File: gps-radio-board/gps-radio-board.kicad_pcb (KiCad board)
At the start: 2 copper layers, 32 x 48 mm, 10 parts, among them J1 Conn_Coaxial_Small, J2 Conn_01x02, J3 USB_C_Receptacle_USB2.0_16P, J4 Conn_Coaxial_Small, U1 ESP32-C6-MINI-1U-H4, U3 AP2112K-3.3, U4 AP2112K-3.3

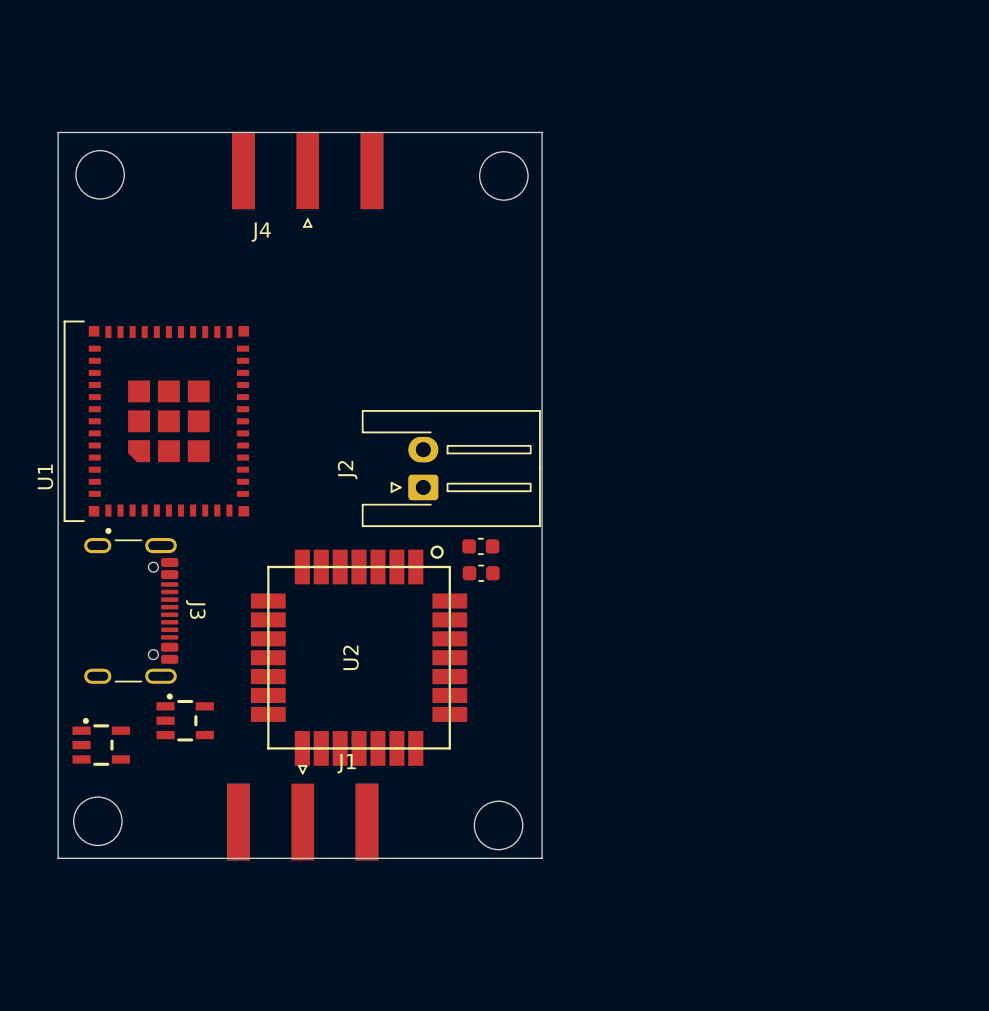
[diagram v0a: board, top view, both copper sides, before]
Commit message: Add components to schematic
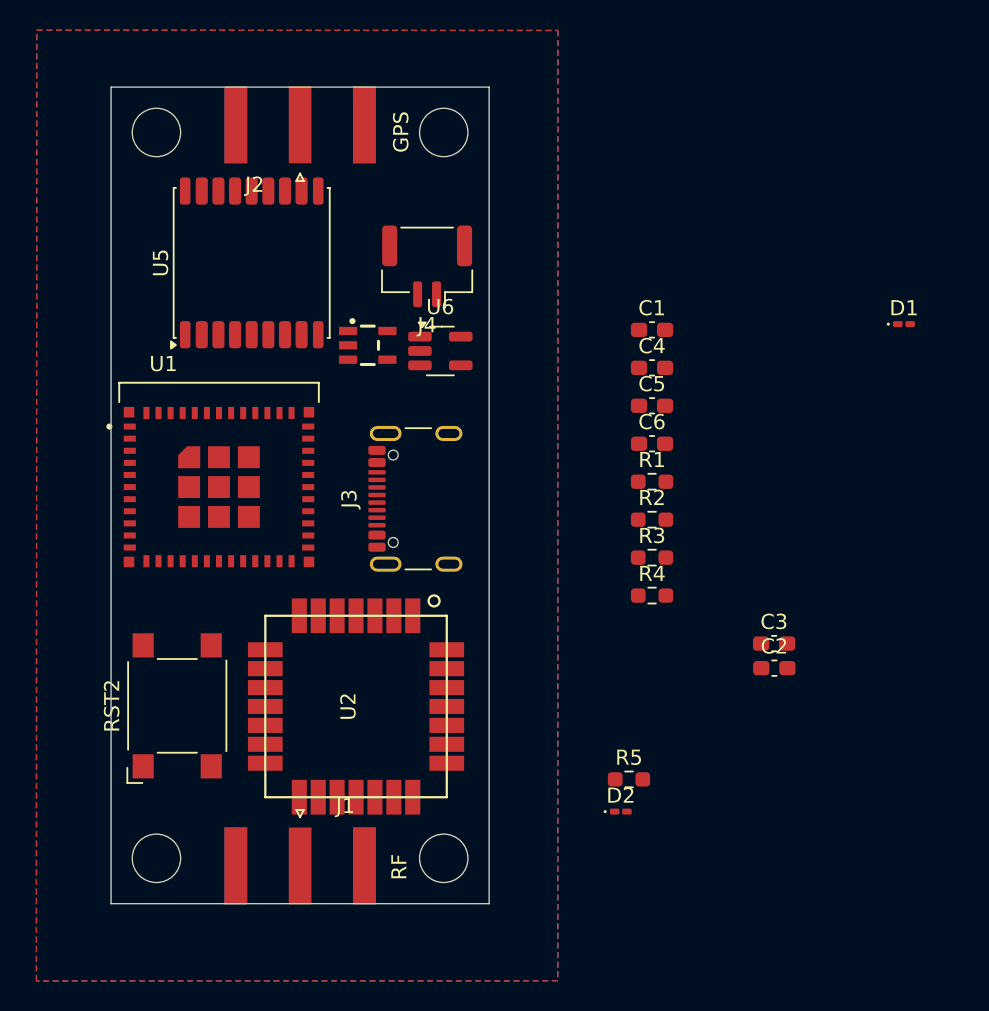
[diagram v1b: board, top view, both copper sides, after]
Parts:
- removed U3: AP2112K-3.3, PCM_SparkFun-Semiconductor-Standard:SOT23-5
- added C1: 4.7u, Capacitor_SMD:C_0603_1608Metric_Pad1.08x0.95mm_HandSolder, F.Cu at (123.3, 89.1)
- added C4: 4.7u, Capacitor_SMD:C_0603_1608Metric_Pad1.08x0.95mm_HandSolder, F.Cu at (123.3, 91.6)
- added C5: 4.7u, Capacitor_SMD:C_0603_1608Metric_Pad1.08x0.95mm_HandSolder, F.Cu at (123.3, 94.1)
- added C6: 4.7u, Capacitor_SMD:C_0603_1608Metric_Pad1.08x0.95mm_HandSolder, F.Cu at (123.3, 96.6)
- added D1: LED, LED_SMD:LED_0201_0603Metric_Pad0.64x0.40mm_HandSolder, F.Cu at (139.9, 88.7)
- added D2: LED, LED_SMD:LED_0201_0603Metric_Pad0.64x0.40mm_HandSolder, F.Cu at (121.2, 120.9)
- added R1: 2k, Resistor_SMD:R_0603_1608Metric_Pad0.98x0.95mm_HandSolder, F.Cu at (123.3, 99.1)
- added R2: 470, Resistor_SMD:R_0603_1608Metric_Pad0.98x0.95mm_HandSolder, F.Cu at (123.3, 101.6)
- added R3: 5.1k, Resistor_SMD:R_0603_1608Metric_Pad0.98x0.95mm_HandSolder, F.Cu at (123.3, 104.1)
- added R4: 5.1k, Resistor_SMD:R_0603_1608Metric_Pad0.98x0.95mm_HandSolder, F.Cu at (123.3, 106.6)
- added R5: 470, Resistor_SMD:R_0603_1608Metric_Pad0.98x0.95mm_HandSolder, F.Cu at (121.8, 118.8)
- added RST2: SW_Omron_B3FS, Button_Switch_SMD:SW_SPST_Omron_B3FS-100xP, F.Cu at (91.9, 113.9)
- added U5: MAX-M10N, gps-radio-board:ublox_MAX, F.Cu at (96.8, 84.6)
- added U6: MCP73831, Package_TO_SOT_SMD:SOT-23-5_HandSoldering, F.Cu at (109.3, 90.5)
- C2: value 10u -> 100n; footprint PCM_SparkFun-Capacitor:C_0603_1608Metric -> Capacitor_SMD:C_0603_1608Metric_Pad1.08x0.95mm_HandSolder
- C3: value 100n -> 10u; footprint PCM_SparkFun-Capacitor:C_0603_1608Metric -> Capacitor_SMD:C_0603_1608Metric_Pad1.08x0.95mm_HandSolder
- J1: value Conn_Coaxial_Small -> SMA
- J2: value Conn_01x02 -> SMA; footprint Connector_JST:JST_XH_S2B-XH-A-1_1x02_P2.50mm_Horizontal -> Connector_Coaxial:SMA_Amphenol_132289_EdgeMount
- J4: value Conn_Coaxial_Small -> JST_BATT; footprint Connector_Coaxial:SMA_Amphenol_132289_EdgeMount -> Connector_JST:JST_GH_SM02B-GHS-TB_1x02-1MP_P1.25mm_Horizontal
- moved U4 27.6 mm to (104.5, 90.1)
- moved J2 25.3 mm to (100.0, 75.5)
- moved J3 22.3 mm to (108.8, 100.2), turned to 90 degrees
- moved C3 20.4 mm to (131.3, 109.8)
- moved C2 20.4 mm to (131.4, 111.4)
- moved J4 10.1 mm to (108.4, 84.8), turned to 180 degrees
- moved U1 5.47 mm to (94.6, 99.5), turned to 0 degrees
- moved U2 3.23 mm to (103.7, 114.0)
- moved J1 2.91 mm to (100.0, 124.5)
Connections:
- net Net-(J3-VBUS-PadA4) renamed /USB_IN
- C2 pad 1: unconnected-(C2-Pad1) -> +3V3
- C2 pad 2: unconnected-(C2-Pad2) -> GND
- C3 pad 1: unconnected-(C3-Pad1) -> +3V3
- C3 pad 2: unconnected-(C3-Pad2) -> GND
- J2 pad 1: GND -> Net-(J2-In)
- J2 pad 2: Net-(J2-Pin_2) -> GND
- J3 pad A1: Net-(J3-GND-PadA1) -> GND
- J3 pad A12: Net-(J3-GND-PadA1) -> GND
- J3 pad A5: unconnected-(J3-CC1-PadA5) -> Net-(J3-CC1)
- J3 pad A6: unconnected-(J3-D+-PadA6) -> /USB_D+
- J3 pad A7: unconnected-(J3-D--PadA7) -> /USB_D-
- J3 pad B1: Net-(J3-GND-PadA1) -> GND
- J3 pad B12: Net-(J3-GND-PadA1) -> GND
- J3 pad B5: unconnected-(J3-CC2-PadB5) -> Net-(J3-CC2)
- J3 pad B6: unconnected-(J3-D+-PadB6) -> /USB_D+
- J3 pad B7: unconnected-(J3-D--PadB7) -> /USB_D-
- J3 pad SH: unconnected-(J3-SHIELD-PadSH) -> GND
- J4 pad 1: unconnected-(J4-In-Pad1) -> GND
- J4 pad 2: unconnected-(J4-Ext-Pad2) -> +BATT
- U1 pad 17: unconnected-(U1-IO12-Pad17) -> /USB_D-
- U1 pad 18: unconnected-(U1-IO13-Pad18) -> /USB_D+
- U1 pad 30: unconnected-(U1-RXD0-Pad30) -> /WIO_UART_2_TX
- U1 pad 31: unconnected-(U1-TXD0-Pad31) -> /WIO_UART_2_RX
- U1 pad 6: unconnected-(U1-IO3-Pad6) -> Net-(D2-A)
- U2 pad 10: unconnected-(U2-PB6-Pad10) -> /WIO_UART_1_TX
- U2 pad 11: unconnected-(U2-PB5-Pad11) -> /SPI-COTI
- U2 pad 12: unconnected-(U2-PC1-Pad12) -> /I2C-2-SCA
- U2 pad 13: unconnected-(U2-PC0-Pad13) -> /I2C-2-SCL
- U2 pad 18: unconnected-(U2-PA3-Pad18) -> /WIO_UART_2_RX
- U2 pad 19: unconnected-(U2-PA2-Pad19) -> /WIO_UART_2_TX
- U2 pad 20: unconnected-(U2-PB10-Pad20) -> /EXT_INT_GPS
- U2 pad 23: unconnected-(U2-PA0-Pad23) -> /SPI-CS
- U2 pad 3: unconnected-(U2-PA13-Pad3) -> /SWD-WIO-IO
- U2 pad 4: unconnected-(U2-PA14-Pad4) -> /SWD-WIO-CLK
- U2 pad 5: unconnected-(U2-PB15-Pad5) -> /I2C-1-SCL
- U2 pad 6: unconnected-(U2-PA15-Pad6) -> /I2C-1-SDA
- U2 pad 7: unconnected-(U2-PB4-Pad7) -> /SPI-CITO
- U2 pad 8: unconnected-(U2-PB3-Pad8) -> /SPI-SCK
- U2 pad 9: unconnected-(U2-PB7-Pad9) -> /WIO_UART_1_RX
- U4 pad 1: unconnected-(U4-VIN-Pad1) -> +BATT
- U4 pad 2: unconnected-(U4-GND-Pad2) -> GND
- U4 pad 3: unconnected-(U4-EN-Pad3) -> +BATT
- U4 pad 5: unconnected-(U4-VOUT-Pad5) -> +3V3
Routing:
- added copper zone on In2.Cu, net +3V3
- added copper zone on B.Cu, net GND
- added copper zone on F.Cu, net GND
- added copper zone on In1.Cu, net GND
- added copper zone on In2.Cu, net GND
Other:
- board size 32 x 48 mm -> 25 x 54 mm
- copper layers 2 -> 4
- board text added: "GPS"
- board text added: "RF"

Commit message: Inital components in schematic
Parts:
- added C10: 22u, Capacitor_SMD:C_0603_1608Metric_Pad1.08x0.95mm_HandSolder, F.Cu at (136.8, 103.8)
- added C7: 1u, Capacitor_SMD:C_0603_1608Metric_Pad1.08x0.95mm_HandSolder, F.Cu at (136.8, 96.3)
- added C8: 100n, Capacitor_SMD:C_0603_1608Metric_Pad1.08x0.95mm_HandSolder, F.Cu at (136.8, 98.8)
- added C9: 100n, Capacitor_SMD:C_0603_1608Metric_Pad1.08x0.95mm_HandSolder, F.Cu at (136.8, 101.3)
- added R6: 10k, Resistor_SMD:R_0603_1608Metric_Pad0.98x0.95mm_HandSolder, F.Cu at (136.8, 106.3)
- added R7: 10k, Resistor_SMD:R_0603_1608Metric_Pad0.98x0.95mm_HandSolder, F.Cu at (136.8, 108.9)
- added U7: AP2112K-3.3, PCM_SparkFun-Semiconductor-Standard:SOT23-5, F.Cu at (141.7, 97.4)
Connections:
- C6 pad 1: +3V3_G -> +3V3_E
- RST2 pad 1: unconnected-(RST2-Pad1) -> GND
- RST2 pad 2: unconnected-(RST2-Pad2) -> Net-(U1-EN)
- U1 pad 22: unconnected-(U1-IO8-Pad22) -> Net-(U1-IO8)
- U1 pad 3: +3V3 -> +3V3_E
- U1 pad 5: unconnected-(U1-IO2-Pad5) -> Net-(U1-IO2)
- U1 pad 8: unconnected-(U1-EN-Pad8) -> Net-(U1-EN)
- U4 pad 3: +BATT -> Net-(U1-IO2)

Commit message: Inital rousting
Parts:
- removed RST2: SW_Omron_B3FS, Button_Switch_SMD:SW_SPST_Omron_B3FS-100xP
- added C11: 15p, Capacitor_SMD:C_0603_1608Metric_Pad1.08x0.95mm_HandSolder, F.Cu at (101.5, 96.3)
- added C12: 15p, Capacitor_SMD:C_0603_1608Metric_Pad1.08x0.95mm_HandSolder, F.Cu at (101.4, 102.7)
- added D3: 40V@1A, Diode_SMD:D_SOD-123, F.Cu at (103.7, 81.4)
- added D4: 40V@1A, Diode_SMD:D_SOD-123, F.Cu at (108.0, 88.2)
- added J5: Conn_01x04, Connector_JST:JST_SH_BM04B-SRSS-TB_1x04-1MP_P1.00mm_Vertical, F.Cu at (91.9, 113.7)
- added J6: Conn_01x04, Connector_JST:JST_SH_BM04B-SRSS-TB_1x04-1MP_P1.00mm_Vertical, F.Cu at (91.8, 119.0)
- added J7: Conn_01x04, Connector_PinHeader_2.54mm:PinHeader_1x04_P2.54mm_Vertical, F.Cu at (89.4, 90.3)
- added R8: 22, Resistor_SMD:R_0603_1608Metric_Pad0.98x0.95mm_HandSolder, F.Cu at (102.3, 98.7)
- added R9: 22, Resistor_SMD:R_0603_1608Metric_Pad0.98x0.95mm_HandSolder, F.Cu at (102.3, 100.2)
- D1, D2: footprint LED_SMD:LED_0201_0603Metric_Pad0.64x0.40mm_HandSolder -> LED_SMD:LED_0603_1608Metric_Pad1.05x0.95mm_HandSolder
- moved C8 49.0 mm to (89.0, 109.3), turned to 90 degrees
- moved C7 48.8 mm to (89.2, 106.8)
- moved C9 45.6 mm to (91.7, 107.8), turned to 90 degrees
- moved R6 45.4 mm to (91.6, 110.3)
- moved C10 43.8 mm to (93.2, 107.8), turned to 90 degrees
- moved R7 38.9 mm to (101.4, 92.8), turned to 90 degrees
- moved U7 38.5 mm to (103.7, 90.9), turned to -90 degrees
- moved C3 29.4 mm to (102.3, 105.7), turned to 180 degrees
- moved D2 29.1 mm to (95.8, 106.9), turned to 180 degrees
- moved D1 28.8 mm to (111.1, 89.5), turned to 90 degrees
- moved R5 28.0 mm to (95.7, 108.5), turned to 180 degrees
- moved C5 24.5 mm to (99.0, 91.4), turned to 180 degrees
- moved R4 22.7 mm to (103.1, 96.3), turned to 90 degrees
- moved C2 20.6 mm to (111.1, 107.5), turned to 90 degrees
- moved R3 20.2 mm to (103.2, 102.8), turned to -90 degrees
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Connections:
- C4 pad 1: +BATT -> Net-(D3-K)
- C5 pad 1: +BATT -> Net-(D3-K)
- J3 pad A6: /USB_D+ -> Net-(J3-D+-PadA6)
- J3 pad A7: /USB_D- -> Net-(J3-D--PadA7)
- J3 pad B6: /USB_D+ -> Net-(J3-D+-PadA6)
- J3 pad B7: /USB_D- -> Net-(J3-D--PadA7)
- U1 pad 10: unconnected-(U1-IO5-Pad10) -> Net-(J7-Pin_3)
- U1 pad 9: unconnected-(U1-IO4-Pad9) -> Net-(J7-Pin_2)
- U4 pad 1: +BATT -> Net-(D3-K)
- U7 pad 1: +BATT -> Net-(D3-K)
- U7 pad 3: +BATT -> Net-(D3-K)
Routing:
- net +3V3_E: track 0.00 -> 43.5 mm
- net Net-(U1-IO2): track 0.00 -> 41.9 mm, vias 0 -> 2
- net /EXT_INT_GPS: track 0.00 -> 37.2 mm, vias 0 -> 2
- net /WIO_UART_2_TX: track 0.00 -> 33.9 mm, vias 0 -> 2
- net /WIO_UART_2_RX: track 0.00 -> 32.8 mm, vias 0 -> 2
- net /WIO_UART_1_TX: track 0.00 -> 30.2 mm, vias 0 -> 2
- net /WIO_UART_1_RX: track 0.00 -> 29.0 mm, vias 0 -> 2
- net /USB_IN: track 0.00 -> 28.7 mm
- net /SWD-WIO-IO: track 0.00 -> 26.0 mm, vias 0 -> 2
- net /SWD-WIO-CLK: track 0.00 -> 24.7 mm, vias 0 -> 2
- net +3V3: track 0.00 -> 24.2 mm, vias 0 -> 9
- net Net-(J7-Pin_3): track 0.00 -> 24.0 mm, vias 0 -> 2
- net +BATT: track 0.00 -> 23.3 mm
- net Net-(J7-Pin_2): track 0.00 -> 21.3 mm, vias 0 -> 2
- net Net-(U1-EN): track 0.00 -> 19.4 mm
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
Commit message: Update silkscreen
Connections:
- J5 pad 1: +3V3 -> /SWD-WIO-IO
- J5 pad 2: /SWD-WIO-IO -> /SWD-WIO-CLK
- J5 pad 3: /SWD-WIO-CLK -> +3V3
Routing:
- net /SWD-WIO-IO: track 26.0 -> 27.1 mm
- net /SWD-WIO-CLK: track 24.7 -> 25.6 mm
- net GND: vias 90 -> 91
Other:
- board text added: "3V3"
- board text added: "GND"
- board text added: "I2C"
- board text added: "PWR"
- board text added: "RX"
- board text added: "SWD"
- board text added: "TX"
- board text added: "Telemetry In Midair 1"

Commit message: Update silkscreen
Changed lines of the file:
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@@
 		(tags "SOD-123")
 		(property "Reference" "D4"
-			(at 0 -2 0)
+			(at -2.7 0.5 90)
 			(layer "F.SilkS")
 			(effects
@@
 		(tags "capacitor handsolder")
 		(property "Reference" "C1"
-			(at 1.25 0.8 0)
+			(at -1.375 0.825 0)
 			(layer "F.SilkS")
 			(effects
@@
 		(at 103.8 113.958677 -90)
 		(property "Reference" "U2"
-			(at 0 0.5 90)
+			(at 6.541323 -5.35 0)
 			(layer "F.SilkS")
 			(effects
@@
 		(tags "Through hole pin header THT 1x04 2.54mm single row")
 		(property "Reference" "J7"
-			(at 3.475 3.775 0)
+			(at -0.075 9.525 0)
 			(layer "F.SilkS")
 			(effects
@@
 		(tags "LED handsolder")
 		(property "Reference" "D1"
-			(at 0 -1.43 90)
+			(at 2.025 0.45 0)
 			(layer "F.SilkS")
 			(effects
@@
 		)
 	)
-	(gr_text "TX"
-		(at 91.45 86.025 90)
+	(gr_text "GND"
+		(at 91.475 83.375 90)
 		(layer "F.SilkS")
 		(effects
@@
 		)
 	)
-	(gr_text "GND"
-		(at 91.475 83.375 90)
+	(gr_text "TX"
+		(at 91.475 85.75 90)
 		(layer "F.SilkS")
 		(effects

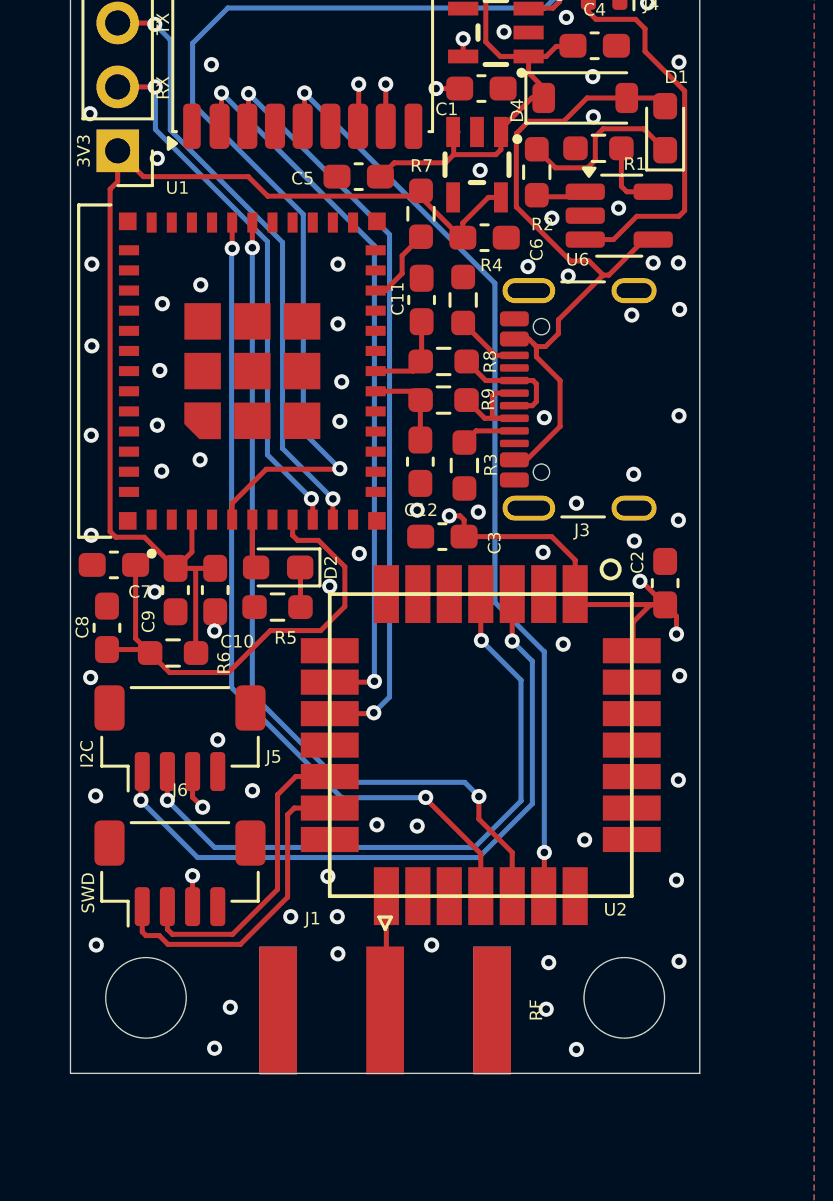
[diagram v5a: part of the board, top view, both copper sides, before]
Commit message: Add leds. Add current ratings
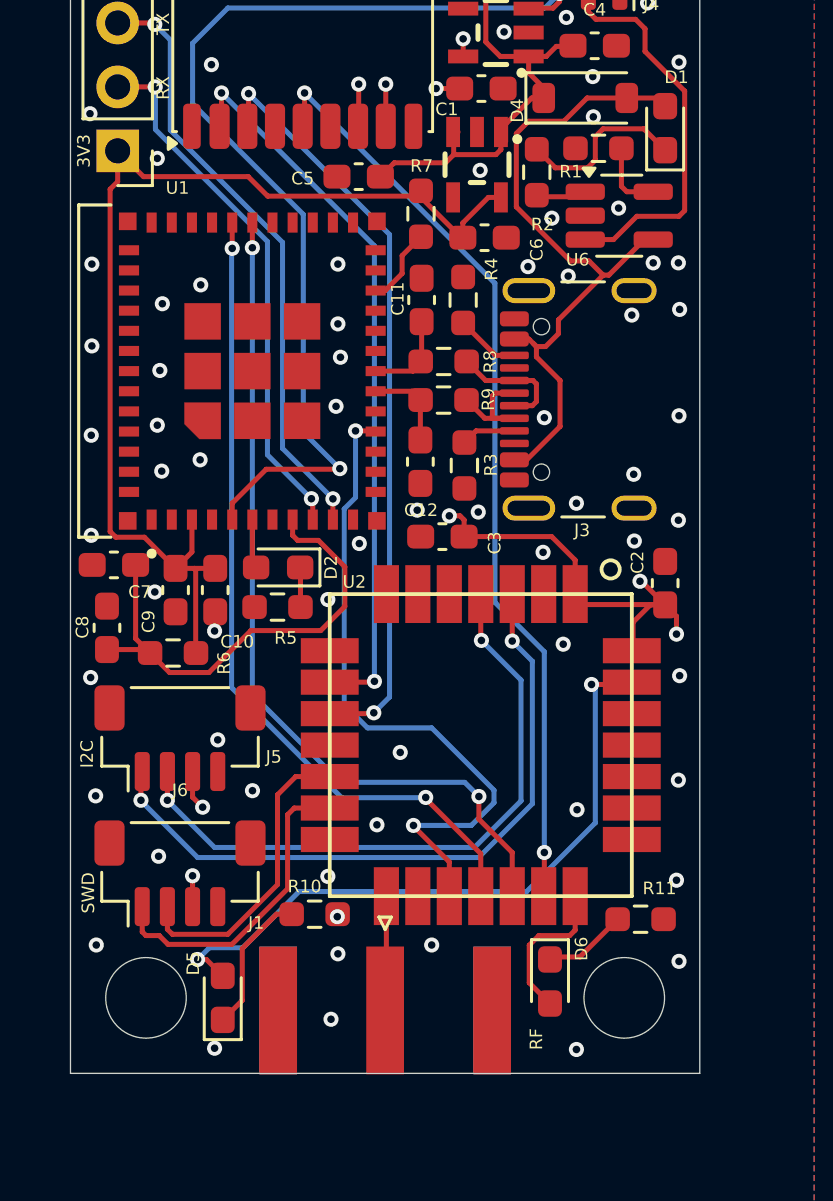
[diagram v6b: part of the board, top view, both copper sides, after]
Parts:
- added D5: LED, LED_SMD:LED_0603_1608Metric_Pad1.05x0.95mm_HandSolder, F.Cu at (93.5, 124.0)
- added D6: LED, LED_SMD:LED_0603_1608Metric_Pad1.05x0.95mm_HandSolder, F.Cu at (106.5, 123.3)
- added R10: 470, Resistor_SMD:R_0603_1608Metric_Pad0.98x0.95mm_HandSolder, F.Cu at (97.2, 120.7)
- added R11: 470, Resistor_SMD:R_0603_1608Metric_Pad0.98x0.95mm_HandSolder, F.Cu at (110.2, 120.9)
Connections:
- U1 pad 15: unconnected-(U1-IO6-Pad15) -> Net-(U1-IO6)
- U2 pad 17: unconnected-(U2-RST-Pad17) -> Net-(U1-IO6)
- U2 pad 21: unconnected-(U2-PA9-Pad21) -> Net-(D6-A)
- U2 pad 27: unconnected-(U2-PA10-Pad27) -> Net-(D5-A)
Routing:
- net Net-(U1-IO6): track 0.00 -> 26.7 mm, vias 0 -> 2
- net Net-(D5-A): track 0.00 -> 26.5 mm, vias 0 -> 2
- net Net-(D6-A): track 0.00 -> 6.18 mm
- net Net-(D5-K): track 0.00 -> 5.69 mm
- net Net-(D6-K): track 0.00 -> 3.31 mm
- net GND: vias 91 -> 89
